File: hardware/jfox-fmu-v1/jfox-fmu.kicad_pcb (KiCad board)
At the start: 6 copper layers, 100 x 80 mm, 140 parts, among them J1 TELEM1, J10 SAFETY, J11 PWM_OUT, J2 TELEM2, J3 GPS1, J30 USB-C, J31 microSD, J4 GPS2, J5 RC_IN, J6 DEBUG, J7 SPI_EXT, J8 PWR_BRICK, J9 PWR_SERVO, Q1A PMOS, Q1B PMOS, Q2A PMOS, Q2B PMOS, Q3A PMOS, Q3B PMOS, U1 ICM-42688-P, U10 STM32H753IIT6, U2 ICM-45686, U20 LTC4417CGN, U21 TPS62132, U22 AP2112K-3.3, U23 AP22804AW5, U24 AP22804AW5, U25 AP22804AW5, U26 AP22804AW5, U3 BMI088, U30 ISOW1044, U31 ISOW1044, U4 BMP388, U40 USBLC6-2SC6, U5 FM25V02A, U6 BMM150, U7 ICP-20100, X1 16MHz, X2 32.768kHz

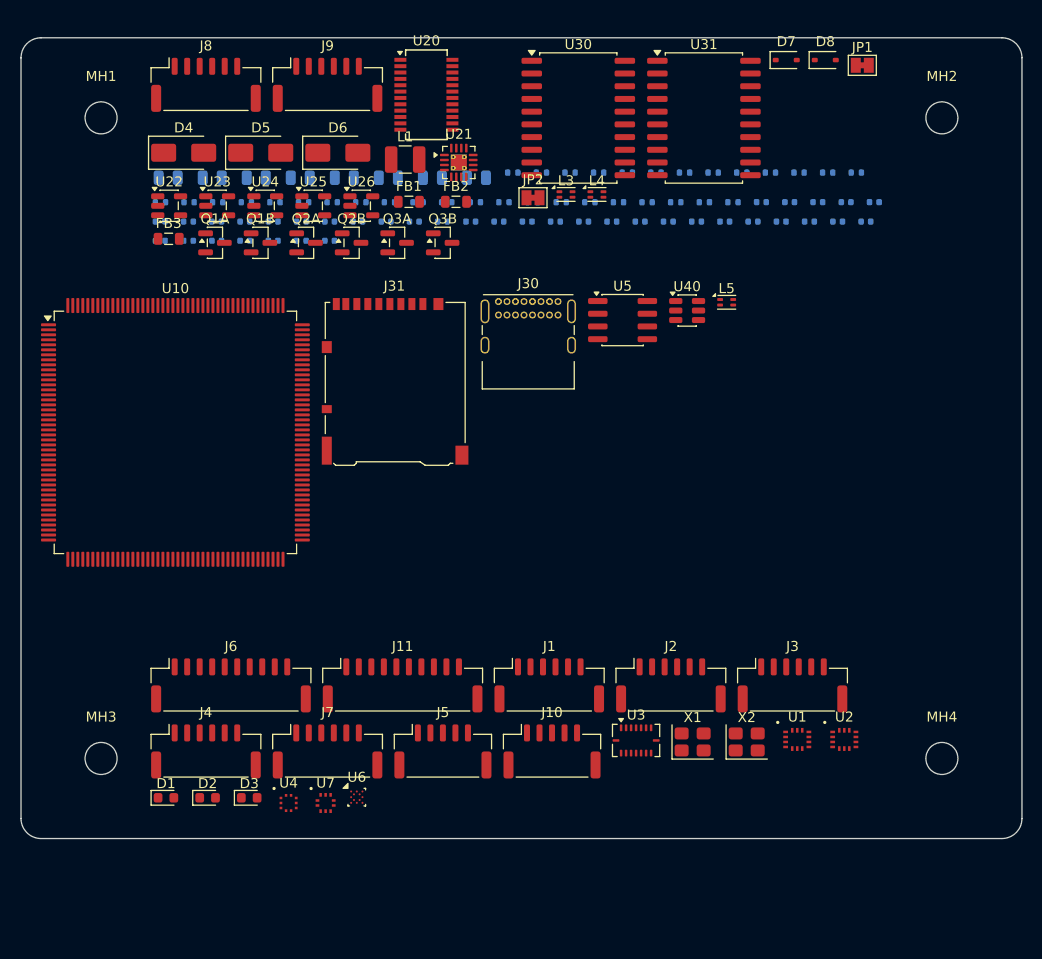
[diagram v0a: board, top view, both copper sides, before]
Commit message: Mezzanine to the carrier, microSD on the edge, sensors moved clear
Three placement changes, and the third is now measured rather than asserted.

QUICK ASSEMBLY. Ten JST-GH headers become one 60-way 0.5 mm mezzanine
(DF12C3.0-60DS) to the carrier, which is what ARCHITECTURE.md already argued
for: eleven looms is eleven things to make, inspect and vibrate loose.
Grounds are interleaved between signal groups rather than grouped at one end,
because a 60-pin connector with no local return is the worst discontinuity on
a board.

What deliberately does NOT cross it: the isolated CAN. A 0.5 mm pitch gives
about 0.5 mm of creepage between adjacent contacts, so running CAN1_H/L
alongside board-referenced signals would quietly reduce the isolation barrier
to that gap - which defeats the ISOW1044 entirely. CAN keeps dedicated
connectors on the isolated side. Debug, USB and the card slot also stay on the
module, because they are used at the module: putting them on the carrier means
unbolting the aircraft to read a log.

The three ferrites became one. Every harness now leaves through the mezzanine,
so there is one 5 V feed to filter instead of three - and three ferrites
driving nets nothing connects to is worse than none.

MICROSD ON THE EDGE, aligned by COURTYARD rather than origin. The first
attempt placed it by its origin and hung a 15 mm deep socket off the board.
The card now ejects outward, off the board, not into U10.

SENSORS MOVED, and the reason checked. The mezzanine freed ten headers' worth
of edge, so the sensors get a dedicated island in the bottom-left - the corner
furthest from both the buck at top-left and the isolated converters at
top-right. The magnetometer is placed by hand in the far corner rather than
packed, because DO-160G s15 makes it the most placement-sensitive part here.

check_fmu_placement.py measures it. "Keep the sensors away from the noise" is
obviously right, impossible to argue with, and untestable as written. Each
sensitive part now has a mini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
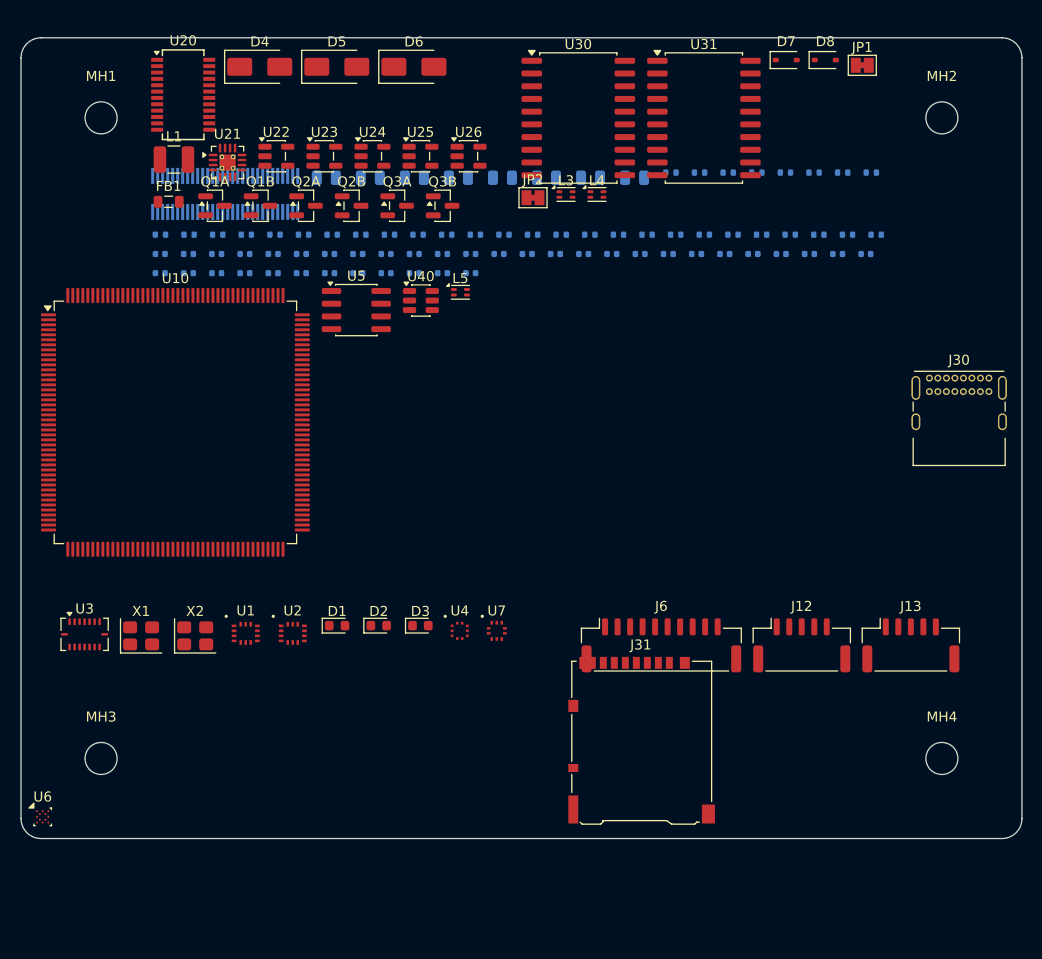
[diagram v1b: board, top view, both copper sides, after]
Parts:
- removed FB2, FB3: 600R@100MHz, L_0805_2012Metric
- removed J1: TELEM1, JST_GH_SM06B-GHS-TB_1x06-1MP_P1.25mm_Horizontal
- removed J10: SAFETY, JST_GH_SM05B-GHS-TB_1x05-1MP_P1.25mm_Horizontal
- removed J11: PWM_OUT, JST_GH_SM10B-GHS-TB_1x10-1MP_P1.25mm_Horizontal
- removed J2: TELEM2, JST_GH_SM06B-GHS-TB_1x06-1MP_P1.25mm_Horizontal
- removed J3: GPS1, JST_GH_SM06B-GHS-TB_1x06-1MP_P1.25mm_Horizontal
- removed J4: GPS2, JST_GH_SM06B-GHS-TB_1x06-1MP_P1.25mm_Horizontal
- removed J5: RC_IN, JST_GH_SM05B-GHS-TB_1x05-1MP_P1.25mm_Horizontal
- removed J7: SPI_EXT, JST_GH_SM06B-GHS-TB_1x06-1MP_P1.25mm_Horizontal
- removed J8: PWR_BRICK, JST_GH_SM06B-GHS-TB_1x06-1MP_P1.25mm_Horizontal
- removed J9: PWR_SERVO, JST_GH_SM06B-GHS-TB_1x06-1MP_P1.25mm_Horizontal
- added J12: CAN1, JST_GH_SM05B-GHS-TB_1x05-1MP_P1.25mm_Horizontal, F.Cu at (108.0, 90.7)
- added J13: CAN2, JST_GH_SM05B-GHS-TB_1x05-1MP_P1.25mm_Horizontal, F.Cu at (118.9, 90.7)
- added J40: DF12C3.0-60DS, Hirose_DF12_DF12C3.0-60DS-0.5V_2x30_P0.50mm_Vertical, B.Cu at (50.4, 45.6)
- moved C1 60.3 mm to (52.4, 51.6)
- moved C45 60.3 mm to (46.7, 51.6)
- moved C2 60.3 mm to (55.2, 51.6)
- moved C44 60.3 mm to (43.9, 51.6)
- moved C46 60.3 mm to (49.5, 51.6)
- moved C30 59.4 mm to (46.7, 53.5)
- moved C32 59.4 mm to (52.4, 53.5)
- moved C29 59.4 mm to (43.9, 53.5)
- moved C31 59.4 mm to (49.5, 53.5)
- moved C33 59.4 mm to (55.2, 53.5)
- moved R28 58.4 mm to (43.9, 49.7)
- moved R3 58.4 mm to (46.8, 49.7)
- moved R4 58.4 mm to (49.6, 49.7)
- moved R5 58.4 mm to (52.5, 49.7)
- moved R6 58.4 mm to (55.4, 49.7)
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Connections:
- FB1 pad 2: +5V_TELEM -> +5V_CARRIER
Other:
- board text added: "EDGE"

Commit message: Card-cage TMR: FCU becomes a plug-in card, backplane carries the I/O
The FMU stops being a module that mates face-to-face with a base board
underneath it and becomes a card that slides into a backplane. That change
came from the JFOX FCU V1 sketch, and it dissolved a constraint I had
worked around rather than removed: the DF12 mezzanine's 3.0 mm stack height
joins two adjacent boards only, so three channels each needing an
independent path to one base board could not use it. Riser cards were the
workaround. Mating at the card's rear edge means nothing has to span the
gap, so the risers and their extra mated pair per channel are gone.

FCU card, 40 x 90 mm (was 100 x 80):
  * 58-contact Samtec MECF-30 card edge, polarised. Contacts 21/22 are a
    1.24 x 7.0 mm key notch offset from centre - a card the wrong way round
    physically will not enter, which is the only insertion safeguard that
    works before power is applied. Two grounds were sacrificed for it out of
    twenty rather than any signal.
  * Power input tree (LTC4417, six ORing FETs, dividers, input TVS) and the
    debug header move to the backplane. The card receives an already-ORed,
    already-fused +5V_CARRIER on three fingers.
  * Front edge carries everything a person touches: microSD, USB-C, and two
    lamps flanking it. D1 is hardwired to the rail so it lights with no
    firmware running - a power lamp the MCU drives tells you the MCU is
    alive, which is not what anyone reads it for.
  * Power and isolated blocks moved to the back face. Both noise groups are
    grouped at one end so the sensor island can sit 22 mm clear at the
    other; spread out, every point on an 80 mm body is within 13 mm of
    something switching.

JFOX-BASE-v1 backplane, 100 x 100 mm, new:
  * Three independent card-edge sockets in a column. A bent contact in one
    slot costs one channel; a shared bus would cost all three and leave the
    voter nothing to vote on.
  * Two airframe feeds at opposite corners, ORed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
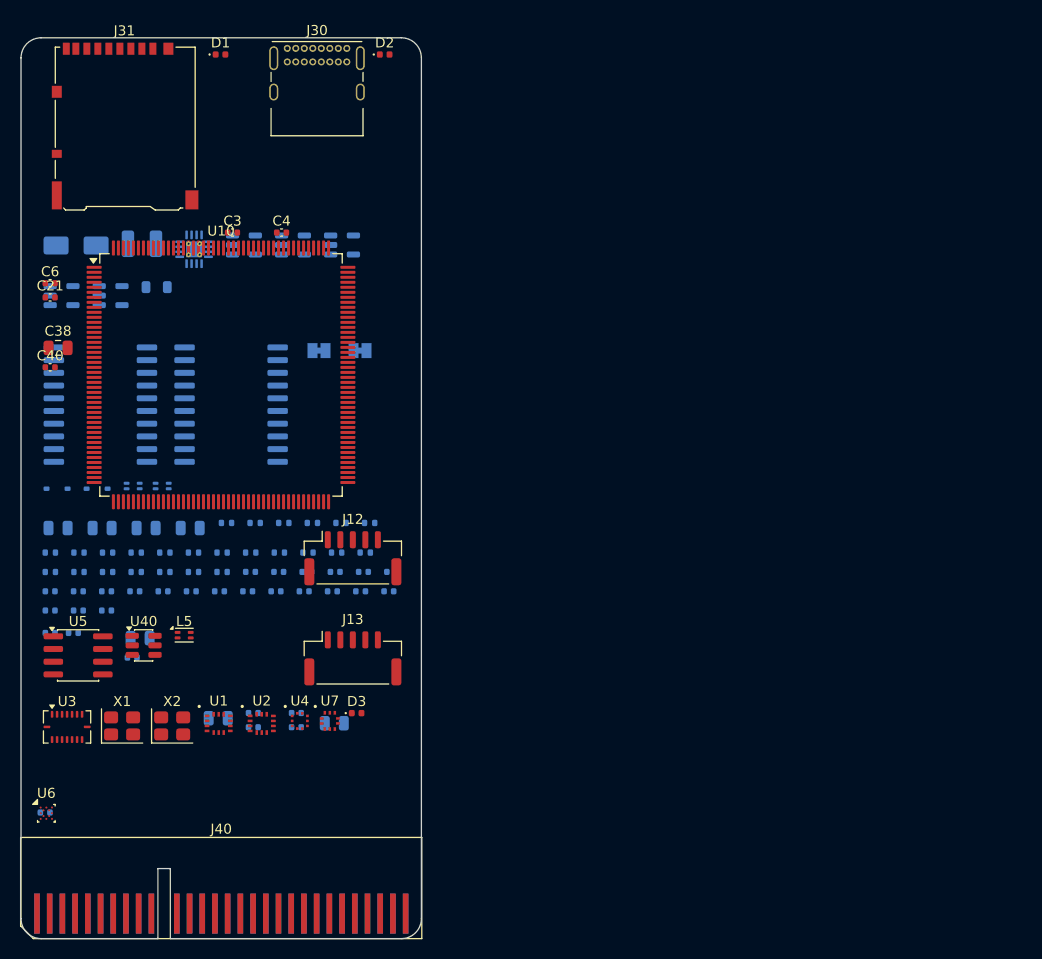
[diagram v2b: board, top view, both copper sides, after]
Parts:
- removed C44, C45, C46: 100n, C_0402_1005Metric
- removed D5, D6: SMAJ6.0A, D_SMA
- removed J6: DEBUG, JST_GH_SM10B-GHS-TB_1x10-1MP_P1.25mm_Horizontal
- removed MH1, MH2, MH3, MH4: M3, MountingHole_3.2mm_M3
- removed Q1A, Q1B, Q2A, Q2B, Q3A, Q3B: PMOS, SOT-23
- removed R20, R23: 787k, R_0402_1005Metric
- removed R21: 49k9, R_0402_1005Metric
- removed R22: 174k, R_0402_1005Metric
- removed R24: 68k1, R_0402_1005Metric
- removed R25: 154k, R_0402_1005Metric
- removed R26: 768k, R_0402_1005Metric
- removed R27: 45k3, R_0402_1005Metric
- removed R28: 182k, R_0402_1005Metric
- removed U20: LTC4417CGN, SSOP-24_3.9x8.7mm_P0.635mm
- C21, C3, C38, C4, C40, C6: moved to F.Cu
- D1: value RED -> PWR-GRN; footprint LED_0603_1608Metric -> LED_0402_1005Metric
- D2: value GRN -> HB-BLU; footprint LED_0603_1608Metric -> LED_0402_1005Metric
- D3: footprint LED_0603_1608Metric -> LED_0402_1005Metric
- D4, D7, D8, FB1, JP1, JP2, L1, L3, L4, U21, U22, U23, U24, U25, U26, U30, U31: moved to B.Cu
- J40: value DF12C3.0-60DS -> CARD EDGE 2x30 P1.27 (no part); footprint Hirose_DF12_DF12C3.0-60DS-0.5V_2x30_P0.50mm_Vertical -> Samtec_MECF-30-0_-L-DV_2x30_P1.27mm_Polarized_Edge; moved to F.Cu
- moved C25 85.2 mm to (35.2, 89.5)
- moved D7 84.5 mm to (33.6, 75.0)
- moved D8 84.4 mm to (37.6, 75.0)
- moved J31 80.2 mm to (40.4, 38.8)
- moved C28 77.3 mm to (53.2, 98.9)
- moved R31 73.5 mm to (32.9, 83.4)
- moved R32 73.5 mm to (35.8, 83.4)
- moved R33 73.5 mm to (38.6, 83.4)
- moved R34 73.5 mm to (41.5, 83.4)
- moved R35 73.5 mm to (44.4, 83.4)
- moved R41 73.5 mm to (47.2, 83.4)
- moved R42 73.5 mm to (50.1, 83.4)
- moved J30 72.1 mm to (56.6, 31.1)
- moved J40 69.4 mm to (50.0, 115.0)
- moved C20 67.9 mm to (38.5, 85.3)
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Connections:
- D1 pad 2: LED_R -> GND
- D4 pad 1: VDD_BRICK -> +5V_CARRIER
- J40 pad 2: VDD_BRICK -> SWDIO
- J40 pad 3: VDD_BRICK -> SWCLK
- J40 pad 5: VDD_SERVO -> NRST
- J40 pad 54: unconnected-(J40-Pin_54-Pad54) -> USART1_RX
- J40 pad 55: unconnected-(J40-Pin_55-Pad55) -> BRICK_VALID
- J40 pad 57: unconnected-(J40-Pin_57-Pad57) -> SERVO_VALID
- J40 pad 58: unconnected-(J40-Pin_58-Pad58) -> USB_VALID
- J40 pad 59: GND -> TIM4_CH4
- J40 pad 6: VDD_SERVO -> USART1_TX
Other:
- board size 100 x 80 mm -> 40 x 90 mm
- rule pad_to_mask_clearance: 0 -> 0.05
- board text added: "DIGITAL2"
- board text removed: "EDGE"

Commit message: FCU DRC to zero: the buck's via array was sitting under the MCU
The sixteen remaining violations were one cause. U21's exposed pad is
stitched to ground by a thermal via array, and it sat on the back face
directly beneath U10 - so its ground vias landed in the MCU's +3V3 pad
field. Opposite sides is not clearance when the part has holes in it.

The search could not have found this. Every candidate it tried left DRC at
16, because the whole NOISY band is under the MCU and no band edge moves a
part out from under a 27 mm package. Confirming that took running the loop
properly, which needed the pattern fix below.

  * band() demanded a ',' after the value it captures, but the last field of
    a ZONES tuple is closed by the paren. So idx 0..2 matched and idx 3 -
    the far edge of every band, the parameter the search needs most - never
    did. Two of six parameters had been silently inert, and the run printed
    "no parameter improved" as though it had searched.
  * The guard that caught it refused to patch rather than editing whichever
    number the regex landed on, which was right. But it exited quietly, and
    a skipped parameter looks identical to a parameter that never helps. It
    now names the pattern and says so.

U21 is pinned rather than packed, clear of three things at once: the MCU
above it, the two CAN landings on the east flank, and 15 mm from the sensor
island. The sensor band moved back 2 mm to give the last 0.5 mm.

The generator now refuses to write a board where a through-hole part
overlaps anything on the far face. This board has three placement paths with
three different ideas of what is occupied - FIXED writes to `where`, the
bottom pass honours `taken`, and zone packing consults nothing at all - and
zone packing has now caused this three times: bands across mounting holes
twice, and a via array across the MCU. Negative-tested by putting U21 back
underneath, which stops the build with the reason.

  check_fmu_drc         PASS   0 blocking
  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
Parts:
- C21: moved to B.Cu
- C22, C7: moved to F.Cu
- moved C21 37.0 mm to (55.5, 85.3)
- moved C7 33.5 mm to (32.9, 53.8)
- moved C22 33.3 mm to (32.9, 55.2)
- moved U21 31.4 mm to (52.1, 82.1)
- moved R19 28.7 mm to (32.9, 83.4)
- moved R30 28.7 mm to (35.8, 83.4)
- moved C6 28.3 mm to (60.8, 49.5)
- moved U25 28.3 mm to (61.9, 50.7)
- moved C24 25.5 mm to (38.5, 87.2)
- moved C39 25.5 mm to (32.9, 87.2)
- moved C42 25.5 mm to (41.4, 87.2)
- moved C9 25.5 mm to (35.7, 87.2)
- moved C18 22.9 mm to (38.5, 85.3)
- moved C19 22.9 mm to (44.2, 85.3)
- moved C31 22.9 mm to (32.9, 85.3)
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
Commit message: JFOX logo as a generated KiCad silkscreen footprint
Converted from hardware/brand/jfox-logo-white.png, which is white artwork on
a transparent background - right for a presentation and wrong for a PCB in
two ways that both silently produce nothing:

  * A tracer reads DARK pixels as the shape, so white-on-transparent
    flattens to white-on-white and converts to an empty footprint.
  * The ALPHA channel carries the artwork. The RGB planes are uniform white
    wherever anything is drawn, so thresholding on brightness keeps the
    background and discards the logo.

So alpha is extracted and inverted. Not bitmap2component: KiCad ships it and
it is the obvious tool, but it is a GUI application that hangs on --help
with no console output, so it cannot be scripted.

Rectangles rather than contours. A contour tracer gives prettier polygons
and then has to solve holes, which KiCad's fp_poly has no primitive for -
and this logo is mostly holes, so every inner contour would fill in.
Rectangle decomposition handles them for free: a hole is simply an absence
of rectangles.

The generator refuses to emit art the fab cannot print. Silkscreen resolves
about 0.15 mm, so one traced pixel must be at least that. At the 8 px/mm I
tried first a pixel is 0.125 mm and 209 of 278 features came out below the
minimum - most of the logo would have arrived as broken speckle rather than
thin. It now stops with the maximum px/mm that works.

Two faults this surfaced:

  * score_fmu_layout raised "no courtyard and no pads" on the logo and took
    the whole scorer down. That guard is right for a component and wrong for
    artwork, which has neither by definition. Keying the skip off the
    board_only attribute did not work - it does not survive into the board
    file - so it keys off having no pads, which is a property of the thing
    rather than a label on it.
  * The logo lands on copper on both boards. Silkscreen over copper is
    clipped by the mask, so a logo placed there does not ap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
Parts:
- added G***: JFOX, JFOX_Logo, F.Cu at (41.0, 78.2)

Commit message: JXK-1 part numbering, from one definition
Format follows MIL-STD-130 UII Construct 2 - enterprise, part number,
serial - and the DO-254 requirement for a correlation between design data
and the as-built article.

  design identifier   JXK-1-1001-A         drawings, BOM, silkscreen
  article identifier  JXK-1-1001-A-0007    one physical unit

Part numbers are blocked so the number says what kind of thing it is:
1000s assemblies, 1100s bare boards, 1200s harnesses, 1300s mechanical,
1400s software, 1500s test equipment.

Two decisions worth recording:

  * An assembly and the bare board it is built on get DIFFERENT part
    numbers. They are different things - one is fabricated, the other
    fabricated and populated - with separate acceptance criteria. The
    SILKSCREEN carries the bare-board number, because silkscreen is applied
    before a single component is fitted and a board claiming the assembly
    number is claiming to be something it is not yet.
  * A serial is never reset when the revision changes and never reused. It
    follows the physical article for life; the revision says what standard
    that article currently conforms to. A serial that restarts per revision
    cannot support the DO-254 correlation at all.

Revision letters skip I, O, Q, S, X and Z - misread as 1, 0, 0, 5, a
cross-out and 2 on a marked board. A change that breaks interchangeability
is a new part number, not a revision; that distinction is the whole value of
the scheme.

part_numbers.py is the single definition and self-checks: block ranges,
excluded revision letters, and that no board uses one number for both its
assembly and its bare board. The schematic revision and title block, and the
board silkscreen, all import from it.

Two faults this surfaced:

  * The schematic generator OVERWROTE jfox-fmu.kicad_pro, which is where the
    PCB generator puts the net classes and design rules - KiCad rejects them
    in the board file. So the order the two happened to run in decided
    w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
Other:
- board text added: "JXK-1-1101-A"
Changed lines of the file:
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@@
 	)
+	)
+	(gr_text "JXK-1-1101-A"
+		(at 32.0 31.6)
+		(layer "F.SilkS")
+		(effects (font (size 0.8 0.8) (thickness 0.12)) (justify left))
 	)
 	(footprint "JFOX_Logo"
